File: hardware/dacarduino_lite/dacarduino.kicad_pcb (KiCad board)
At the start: 2 copper layers, 85 x 64 mm, 42 parts, among them J11 CV IN, J12 CV IN, J13 CV IN, J17 VCC, J18 Vin, J3 CV OUT A, J4 CV OUT B, J5 GATE OUT A, J7 GATE IN, Q1 2N3904, Q3 2N3904, U1 MCP4922, U2 TL972

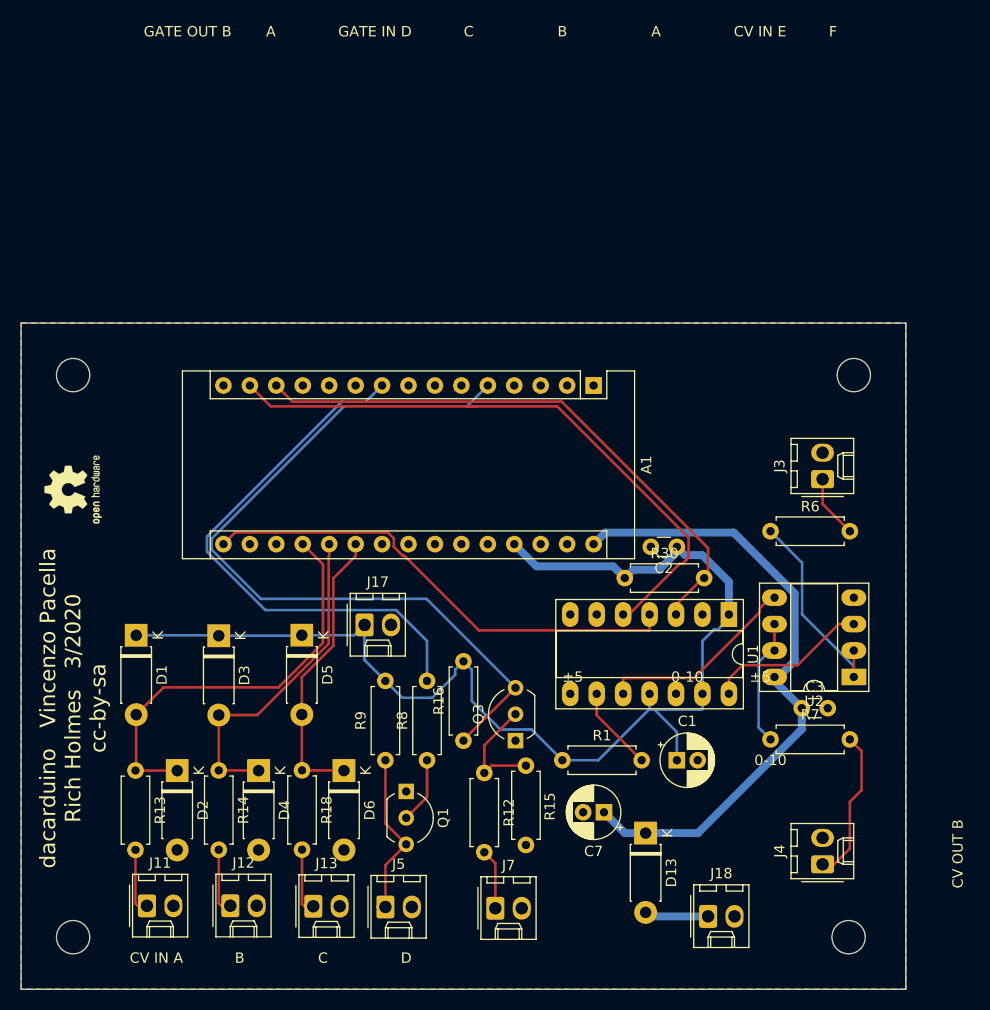
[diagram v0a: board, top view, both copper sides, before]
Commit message: PCB redraw; change op amp selection; revise power tags; move to spaceless directory
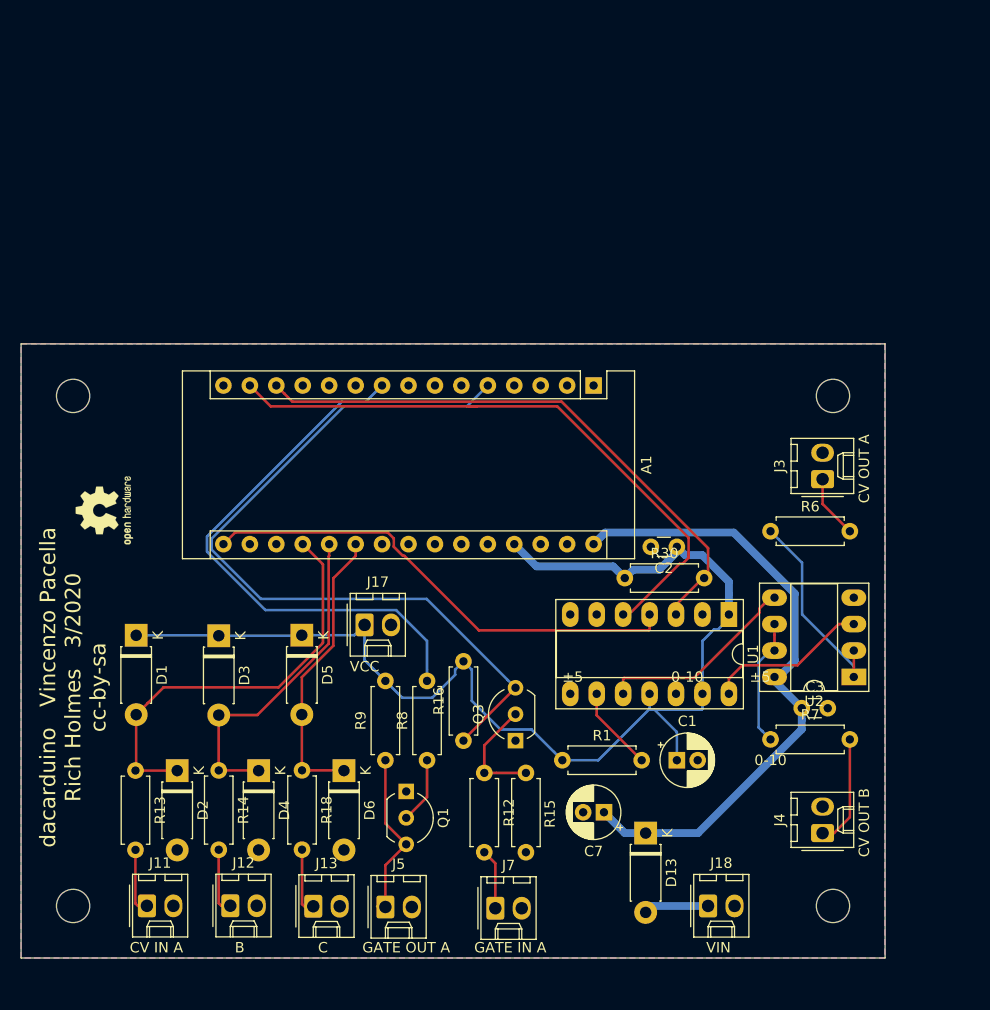
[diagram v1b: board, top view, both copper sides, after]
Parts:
- moved REF** 3.61 mm to (133.0, 109.0)
- moved H4 3.35 mm to (203.0, 147.0)
- moved H2 3.00 mm to (130.0, 147.0)
- moved J4 3.00 mm to (202.0, 140.0)
- moved H3 2.83 mm to (203.0, 98.0)
- moved H1 2.00 mm to (130.0, 98.0)
- moved J18 1.00 mm to (191.0, 147.0)
- moved R15 0.70 mm to (173.5, 141.8)
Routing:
- net /CV out/CV_OUT_B: track 14.7 -> 10.7 mm
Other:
- board size 85 x 64 mm -> 83 x 59 mm
- board text added: "CV OUT A"
- board text added: "GATE IN A"
- board text added: "GATE OUT A"
- board text added: "VCC"
- board text added: "VIN"
- board text removed: "A"
- board text removed: "CV IN E"
- board text removed: "D"
- board text removed: "F"
- board text removed: "GATE IN D"
- board text removed: "GATE OUT B"

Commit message: Backlog of many changes
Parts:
- removed D1, D2, D3, D4, D5, D6: 1N5817, Diode_THT:D_DO-41_SOD81_P7.62mm_Horizontal
- removed J11, J12, J13: CV IN, Connector_Molex:Molex_KK-254_AE-6410-02A_1x02_P2.54mm_Vertical
- removed J7: GATE IN, Connector_Molex:Molex_KK-254_AE-6410-02A_1x02_P2.54mm_Vertical
- removed Q3: 2N3904, Package_TO_SOT_THT:TO-92_Inline_Wide
- removed R12: 100k, Resistor_THT:R_Axial_DIN0207_L6.3mm_D2.5mm_P7.62mm_Horizontal
- removed R13, R14, R18: 1k, Resistor_THT:R_Axial_DIN0207_L6.3mm_D2.5mm_P7.62mm_Horizontal
- removed R15: 1M, Resistor_THT:R_Axial_DIN0207_L6.3mm_D2.5mm_P7.62mm_Horizontal
- removed R16: 10k, Resistor_THT:R_Axial_DIN0207_L6.3mm_D2.5mm_P7.62mm_Horizontal
- removed REF**: OSHW-Logo2_7.3x6mm_SilkScreen, Symbol:OSHW-Logo2_7.3x6mm_SilkScreen
- added J501: Conn_01x04, Connector_Wire:SolderWirePad_1x04_P3.81mm_Drill1.2mm, F.Cu at (155.5, 135.0)
- added J502: Conn_01x04, Connector_Wire:SolderWirePad_1x04_P3.81mm_Drill1.2mm, F.Cu at (130.5, 105.5)
- U301: renamed from U2; value TL972 -> MCP6002
- moved H104 53.0 mm to (184.0, 97.5), turned to 180 degrees
- moved J401 50.5 mm to (169.0, 97.4), turned to 180 degrees
- moved H103 49.8 mm to (184.0, 144.0), turned to 180 degrees
- moved J701 48.8 mm to (158.0, 111.0), turned to 90 degrees
- moved D701 48.0 mm to (154.5, 103.0), turned to 0 degrees
- moved C701 46.5 mm to (159.0, 97.0)
- moved A601 44.6 mm to (135.5, 100.0), turned to 0 degrees
- moved J302 41.9 mm to (181.5, 103.5), turned to 270 degrees
- moved R601 36.4 mm to (161.0, 144.5), turned to 90 degrees
- moved J301 34.7 mm to (181.5, 134.0), turned to 270 degrees
- moved C202 32.7 mm to (161.0, 131.0), turned to 270 degrees
- moved U201 29.3 mm to (166.0, 130.5), turned to 0 degrees
- moved Q401 28.1 mm to (168.0, 108.5), turned to 90 degrees
- moved U301 27.8 mm to (178.5, 116.5), turned to 0 degrees
- moved R301 25.8 mm to (178.5, 129.0)
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- renumbered A1 to A601, C1 to C201, C2 to C202, C3 to C301, C7 to C701, D13 to D701, H1 to H101, H2 to H102, H3 to H103, H4 to H104, J3 to J301, J4 to J302, J5 to J401, J17 to J601, J18 to J701, Q1 to Q401, R1 to R201, R6 to R301, R7 to R302, R8 to R401, R9 to R402, R30 to R601, U1 to U201
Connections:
- net +12V renamed +VIN
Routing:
- net /Arduino/D_IN_A: track 75.5 -> 6.93 mm
- net VCC: track 115.4 -> 83.7 mm
- net /Arduino/SCK: track 47.2 -> 16.3 mm
- net /Arduino/A_IN_A: track 40.5 -> 10.1 mm
- net /Arduino/MOSI: track 59.5 -> 33.7 mm
- net /Arduino/A_IN_B: track 32.1 -> 7.76 mm
- net /Arduino/DAC_CS: track 55.6 -> 33.7 mm
- net /Arduino/A_IN_C: track 27.9 -> 6.63 mm
- net /Arduino/D_OUT_A: track 52.8 -> 73.2 mm
- net +VIN: track 61.6 -> 47.9 mm
- net Net-(Q3-Pad2): track 10.9 -> 0.00 mm
- net Net-(R201-Pad2): track 8.87 -> 18.6 mm
- net /Arduino/D_IN_B: track 0.00 -> 6.40 mm
- net /Inputs/CV in C/CV_IN: track 6.40 -> 0.00 mm
- net /Inputs/CV in B/CV_IN: track 6.35 -> 0.00 mm
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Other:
- board size 83 x 59 mm -> 64 x 55.5 mm
- board text added: "+ VCC"
- board text added: "+ VIN"
- board text added: "A_A A_B A_C A_D"
- board text added: "D_D D_C D_B D_A"
- board text added: "GATE OUT"
- board text removed: "0-10"
- board text removed: "B"
- board text removed: "C"
- board text removed: "CV IN A"
- board text removed: "GATE IN A"
- board text removed: "GATE OUT A"
- board text removed: "VCC"
- board text removed: "VIN"
- board text removed: "±5"

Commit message: Post-prototype tweaks
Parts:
- removed C301: 0.1uF, Capacitor_THT:C_Disc_D3.0mm_W1.6mm_P2.50mm
- removed D701: 1N5817, Diode_THT:D_DO-41_SOD81_P7.62mm_Horizontal
- removed J301: CV OUT A, Connector_Molex:Molex_KK-254_AE-6410-02A_1x02_P2.54mm_Vertical
- removed J302: CV OUT B, Connector_Molex:Molex_KK-254_AE-6410-02A_1x02_P2.54mm_Vertical
- removed R301, R302: 1K, Resistor_THT:R_Axial_DIN0207_L6.3mm_D2.5mm_P7.62mm_Horizontal
- removed U301: MCP6002, Package_DIP:DIP-8_W7.62mm_Socket_LongPads
- added J1: CV OUT A, Connector_Molex:Molex_KK-254_AE-6410-02A_1x02_P2.54mm_Vertical, F.Cu at (181.8, 118.4)
- added J2: CV OUT B, Connector_Molex:Molex_KK-254_AE-6410-02A_1x02_P2.54mm_Vertical, F.Cu at (181.9, 128.0)
- added R2: 1K, Resistor_THT:R_Axial_DIN0207_L6.3mm_D2.5mm_P7.62mm_Horizontal, F.Cu at (178.8, 113.3)
- added R3: 1K, Resistor_THT:R_Axial_DIN0207_L6.3mm_D2.5mm_P7.62mm_Horizontal, F.Cu at (178.8, 135.0)
- moved C4 4.70 mm to (157.1, 101.3), turned to 0 degrees
- renumbered A601 to A1, C201 to C1, C202 to C2, C701 to C4, H101 to H1, H102 to H2, H103 to H3, H104 to H4, J401 to J5, J501 to J6, J502 to J7, J601 to J8, J701 to J9, Q401 to Q1, R201 to R1, R401 to R6, R402 to R7, R601 to R8, U201 to U1
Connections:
- J9 pad 1: Net-(D701-Pad2) -> +VIN
- U1 pad 10: /CV out/DAC_B -> Net-(R3-Pad1)
- U1 pad 14: /CV out/DAC_A -> Net-(R2-Pad1)
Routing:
- net +VIN: track 47.9 -> 18.3 mm
- net /CV out/DAC_B: track 22.6 -> 0.00 mm
- net Net-(R2-Pad1): track 0.00 -> 19.3 mm
- net Net-(R301-Pad1): track 14.6 -> 0.00 mm
- net /CV out/DAC_A: track 13.2 -> 0.00 mm
- net Net-(R302-Pad1): track 12.6 -> 0.00 mm
- net Net-(D701-Pad2): track 10.4 -> 0.00 mm
- net /DAC/CV_OUT_B: track 0.00 -> 9.51 mm
- net /CV out/CV_OUT_B: track 8.73 -> 0.00 mm
- net Net-(R3-Pad1): track 0.00 -> 8.65 mm
- net /CV out/CV_OUT_A: track 7.56 -> 0.00 mm
- net /DAC/CV_OUT_A: track 0.00 -> 7.56 mm
